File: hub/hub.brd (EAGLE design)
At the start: 100 x 80 mm, 42 parts, among them CN1 10118061-5005010LF, CN2 10118061-5005010LF, CN3 10118061-5005010LF, IC1 LM2592HVS-5.0, IC2 AMIS-42700WC, IC3 AMIS-42700WC, IC4 741G11SN74LVC1G11DBVR, IC5 741G11SN74LVC1G11DBVR, IC6 741G11SN74LVC1G11DBVR, IC7 741G11SN74LVC1G11DBVR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

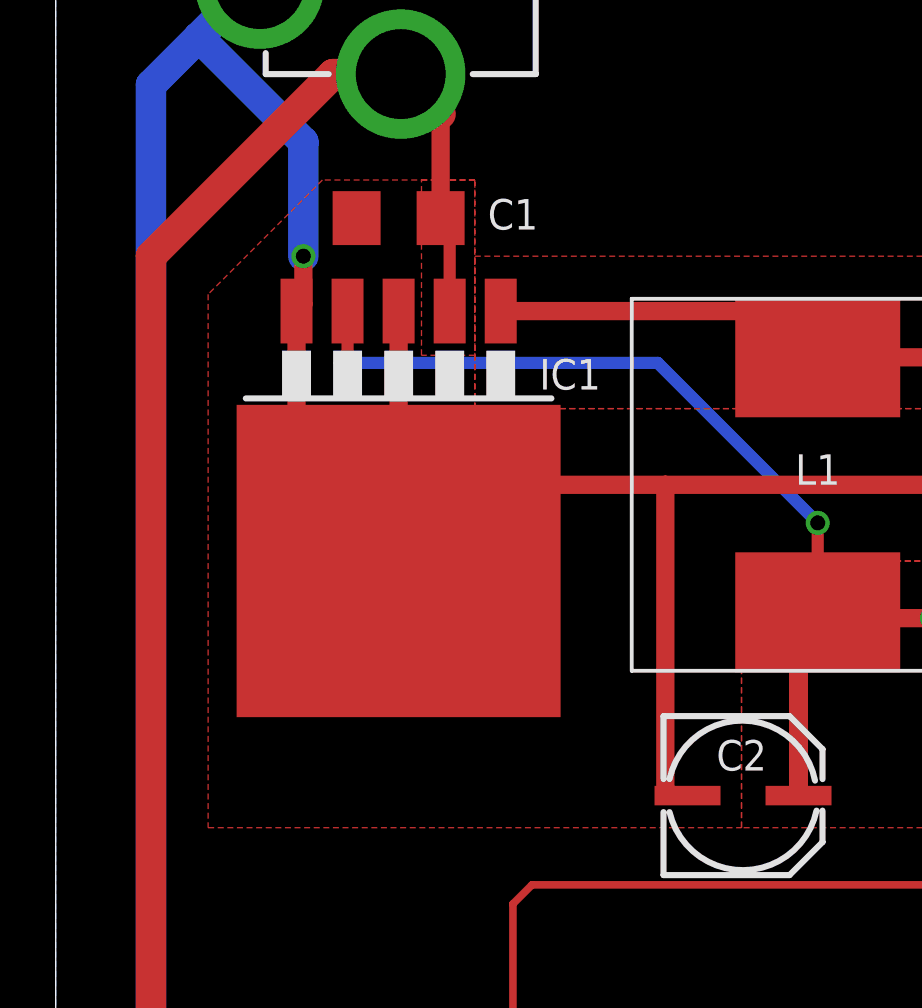
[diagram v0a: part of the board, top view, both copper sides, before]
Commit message: Added beaglebone cape
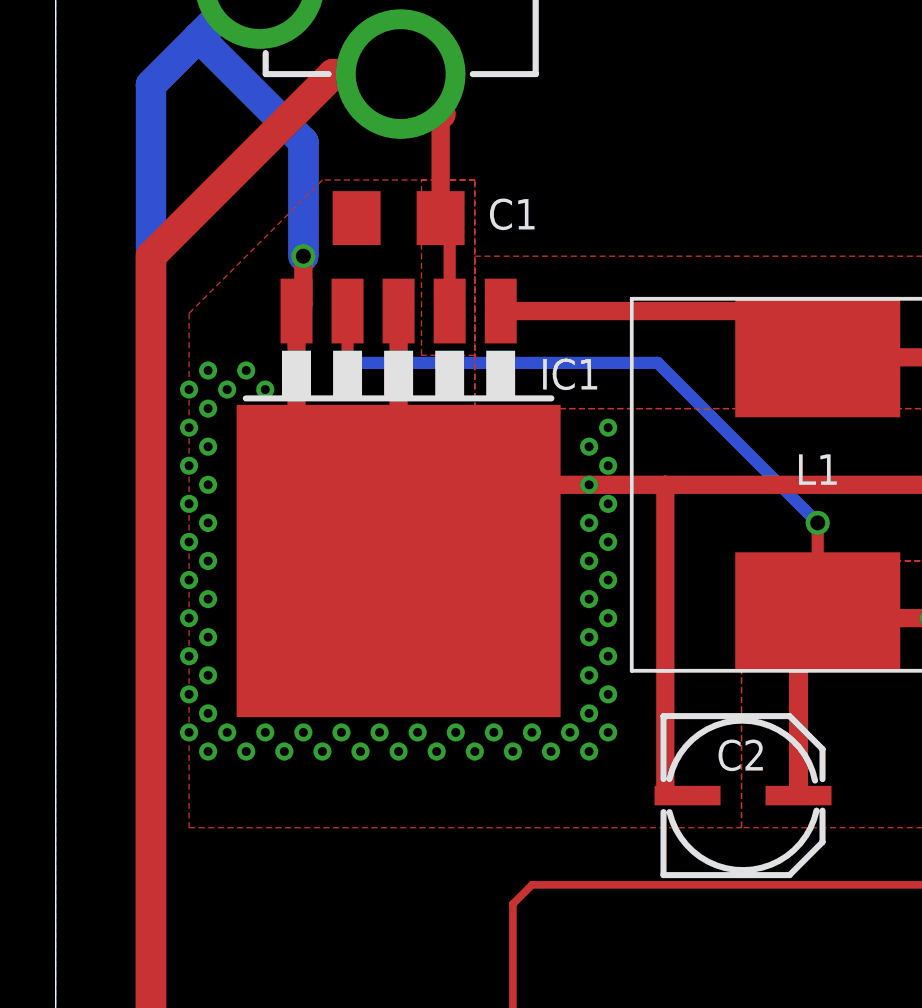
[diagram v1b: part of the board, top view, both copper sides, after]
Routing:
- net GND: vias 12 -> 73
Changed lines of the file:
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@@
 <wire x1="34.29" y1="55.15" x2="34.29" y2="54.61" width="0.6096" layer="1"/>
 <wire x1="34.29" y1="54.61" x2="20.32" y2="54.61" width="0.6096" layer="1"/>
-<wire x1="20.32" y1="54.61" x2="11.43" y2="54.61" width="0.6096" layer="1"/>
+<wire x1="20.32" y1="54.61" x2="17.78" y2="54.61" width="0.6096" layer="1"/>
+<wire x1="17.78" y1="54.61" x2="11.43" y2="54.61" width="0.6096" layer="1"/>
 <wire x1="21.06" y1="44.25" x2="20.52" y2="44.25" width="0.6096" layer="1"/>
 <wire x1="20.52" y1="44.25" x2="20.32" y2="44.45" width="0.6096" layer="1"/>
@@
 <vertex x="13.97" y="64.77"/>
 <vertex x="8.89" y="64.77"/>
-<vertex x="5.08" y="60.96"/>
-<vertex x="5.08" y="43.18"/>
+<vertex x="4.445" y="60.325"/>
+<vertex x="4.445" y="43.18"/>
 <vertex x="22.86" y="43.18"/>
 <vertex x="22.86" y="52.07"/>
@@
 <vertex x="0" y="80.01"/>
 </polygon>
+<via x="6.985" y="57.785" extent="1-16" drill="0.3"/>
+<via x="6.35" y="58.42" extent="1-16" drill="0.3"/>
+<via x="5.715" y="57.785" extent="1-16" drill="0.3"/>
+<via x="5.08" y="58.42" extent="1-16" drill="0.3"/>
+<via x="4.445" y="57.785" extent="1-16" drill="0.3"/>
+<via x="5.08" y="57.15" extent="1-16" drill="0.3"/>
+<via x="4.445" y="56.515" extent="1-16" drill="0.3"/>
+<via x="5.08" y="55.88" extent="1-16" drill="0.3"/>
+<via x="4.445" y="55.245" extent="1-16" drill="0.3"/>
+<via x="5.08" y="54.61" extent="1-16" drill="0.3"/>
+<via x="4.445" y="53.975" extent="1-16" drill="0.3"/>
+<via x="5.08" y="53.34" extent="1-16" drill="0.3"/>
+<via x="4.445" y="52.705" extent="1-16" drill="0.3"/>
+<via x="5.08" y="52.07" extent="1-16" drill="0.3"/>
+<via x="4.445" y="51.435" extent="1-16" drill="0.3"/>
+<via x="5.08" y="50.8" extent="1-16" drill="0.3"/>
+<via x="4.445" y="50.165" extent="1-16" drill="0.3"/>
+<via x="5.08" y="49.53" extent="1-16" drill="0.3"/>
+<via x="4.445" y="48.895" extent="1-16" drill="0.3"/>
+<via x="5.08" y="48.26" extent="1-16" drill="0.3"/>
+<via x="4.445" y="47.625" extent="1-16" drill="0.3"/>
+<via x="5.08" y="46.99" extent="1-16" drill="0.3"/>
+<via x="4.445" y="46.355" extent="1-16" drill="0.3"/>
+<via x="5.08" y="45.72" extent="1-16" drill="0.3"/>
+<via x="5.715" y="46.355" extent="1-16" drill="0.3"/>
+<via x="6.35" y="45.72" extent="1-16" drill="0.3"/>
+<via x="6.985" y="46.355" extent="1-16" drill="0.3"/>
+<via x="7.62" y="45.72" extent="1-16" drill="0.3"/>
+<via x="8.255" y="46.355" extent="1-16" drill="0.3"/>
+<via x="8.89" y="45.72" extent="1-16" drill="0.3"/>
+<via x="9.525" y="46.355" extent="1-16" drill="0.3"/>
+<via x="10.16" y="45.72" extent="1-16" drill="0.3"/>
+<via x="10.795" y="46.355" extent="1-16" drill="0.3"/>
+<via x="11.43" y="45.72" extent="1-16" drill="0.3"/>
+<via x="12.065" y="46.355" extent="1-16" drill="0.3"/>
+<via x="12.7" y="45.72" extent="1-16" drill="0.3"/>
+<via x="13.335" y="46.355" extent="1-16" drill="0.3"/>
+<via x="13.97" y="45.72" extent="1-16" drill="0.3"/>
+<via x="14.605" y="46.355" extent="1-16" drill="0.3"/>
+<via x="15.24" y="45.72" extent="1-16" drill="0.3"/>
+<via x="15.875" y="46.355" extent="1-16" drill="0.3"/>
+<via x="16.51" y="45.72" extent="1-16" drill="0.3"/>
+<via x="17.78" y="45.72" extent="1-16" drill="0.3"/>
+<via x="17.145" y="46.355" extent="1-16" drill="0.3"/>
+<via x="17.78" y="46.99" extent="1-16" drill="0.3"/>
+<via x="18.415" y="47.625" extent="1-16" drill="0.3"/>
+<via x="17.78" y="48.26" extent="1-16" drill="0.3"/>
+<via x="18.415" y="48.895" extent="1-16" drill="0.3"/>
+<via x="17.78" y="49.53" extent="1-16" drill="0.3"/>
+<via x="18.415" y="50.165" extent="1-16" drill="0.3"/>
+<via x="17.78" y="50.8" extent="1-16" drill="0.3"/>
+<via x="18.415" y="51.435" extent="1-16" drill="0.3"/>
+<via x="17.78" y="52.07" extent="1-16" drill="0.3"/>
+<via x="18.415" y="52.705" extent="1-16" drill="0.3"/>
+<via x="17.78" y="53.34" extent="1-16" drill="0.3"/>
+<via x="17.78" y="55.88" extent="1-16" drill="0.3"/>
+<via x="18.415" y="56.515" extent="1-16" drill="0.3"/>
+<via x="17.78" y="54.61" extent="1-16" drill="0.3"/>
+<via x="18.415" y="55.245" extent="1-16" drill="0.3"/>
+<via x="18.415" y="53.975" extent="1-16" drill="0.3"/>
+<via x="18.415" y="46.355" extent="1-16" drill="0.3"/>
 </signal>
 <signal name="SWOUT">
